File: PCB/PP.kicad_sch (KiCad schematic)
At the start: 22 parts, among them J1 USB_B_Micro, Q1 AO4425, Q2 AO3406, Q3 AO4425, Q4 AO3406, U1 ESP32-WROOM-32, U2 DRV8833PWP

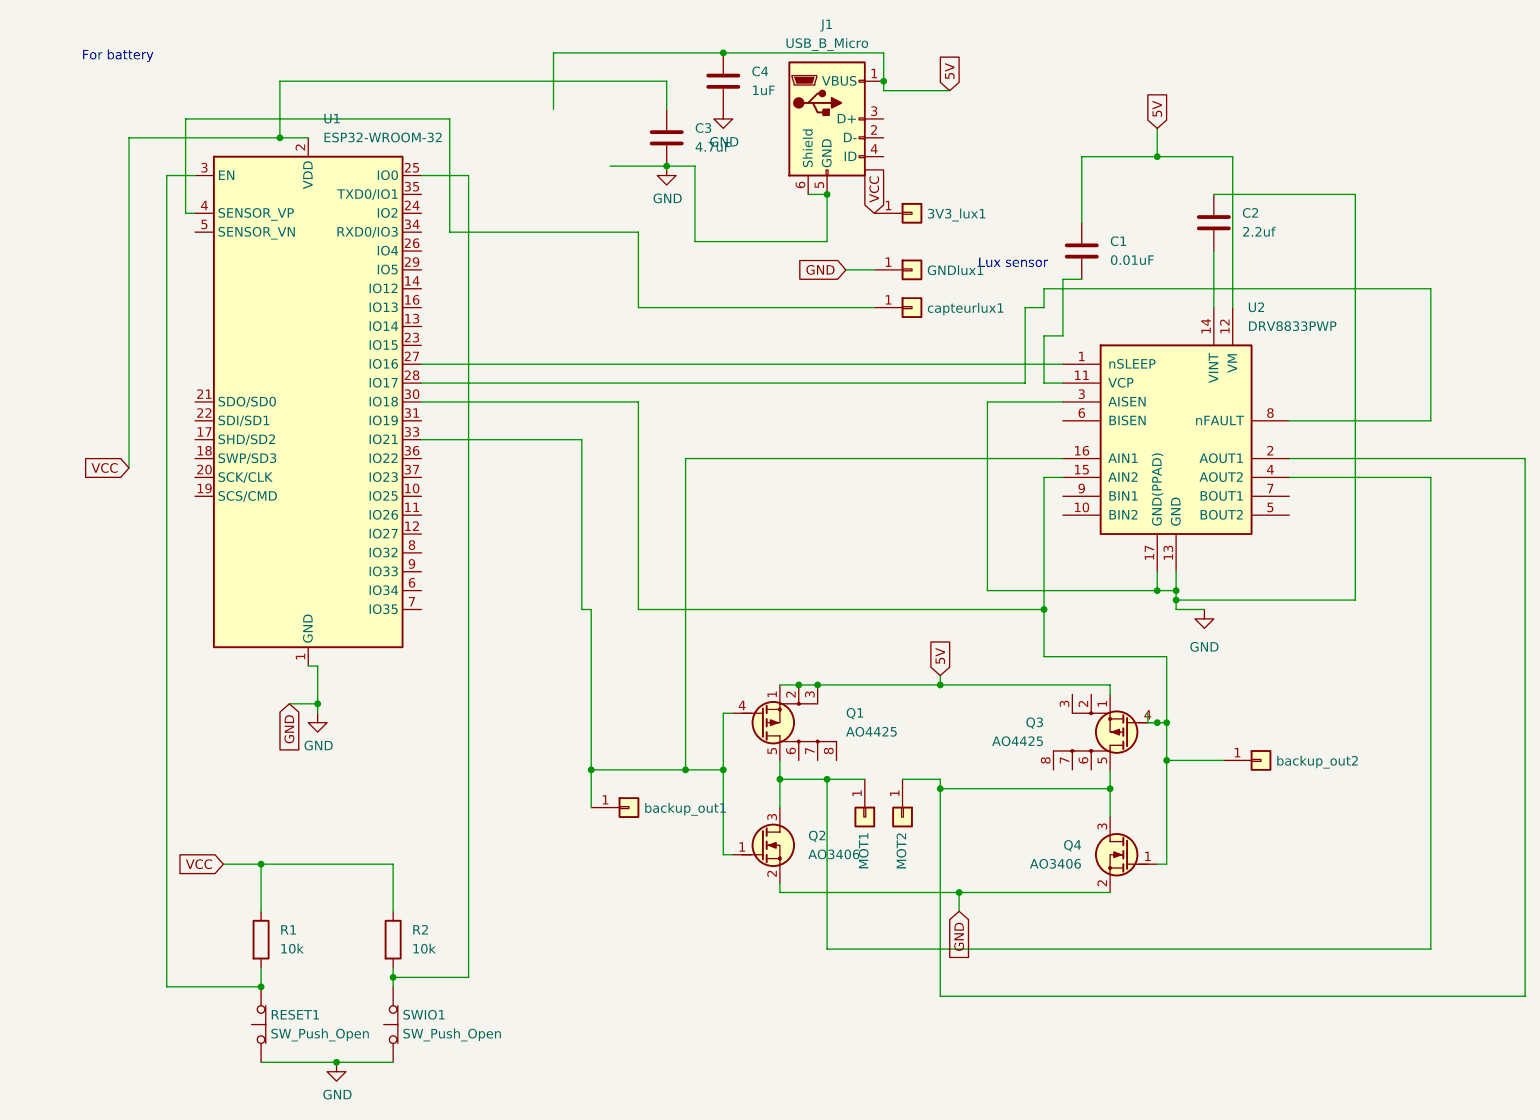
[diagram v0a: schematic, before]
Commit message: adding usb and ap7361 libs
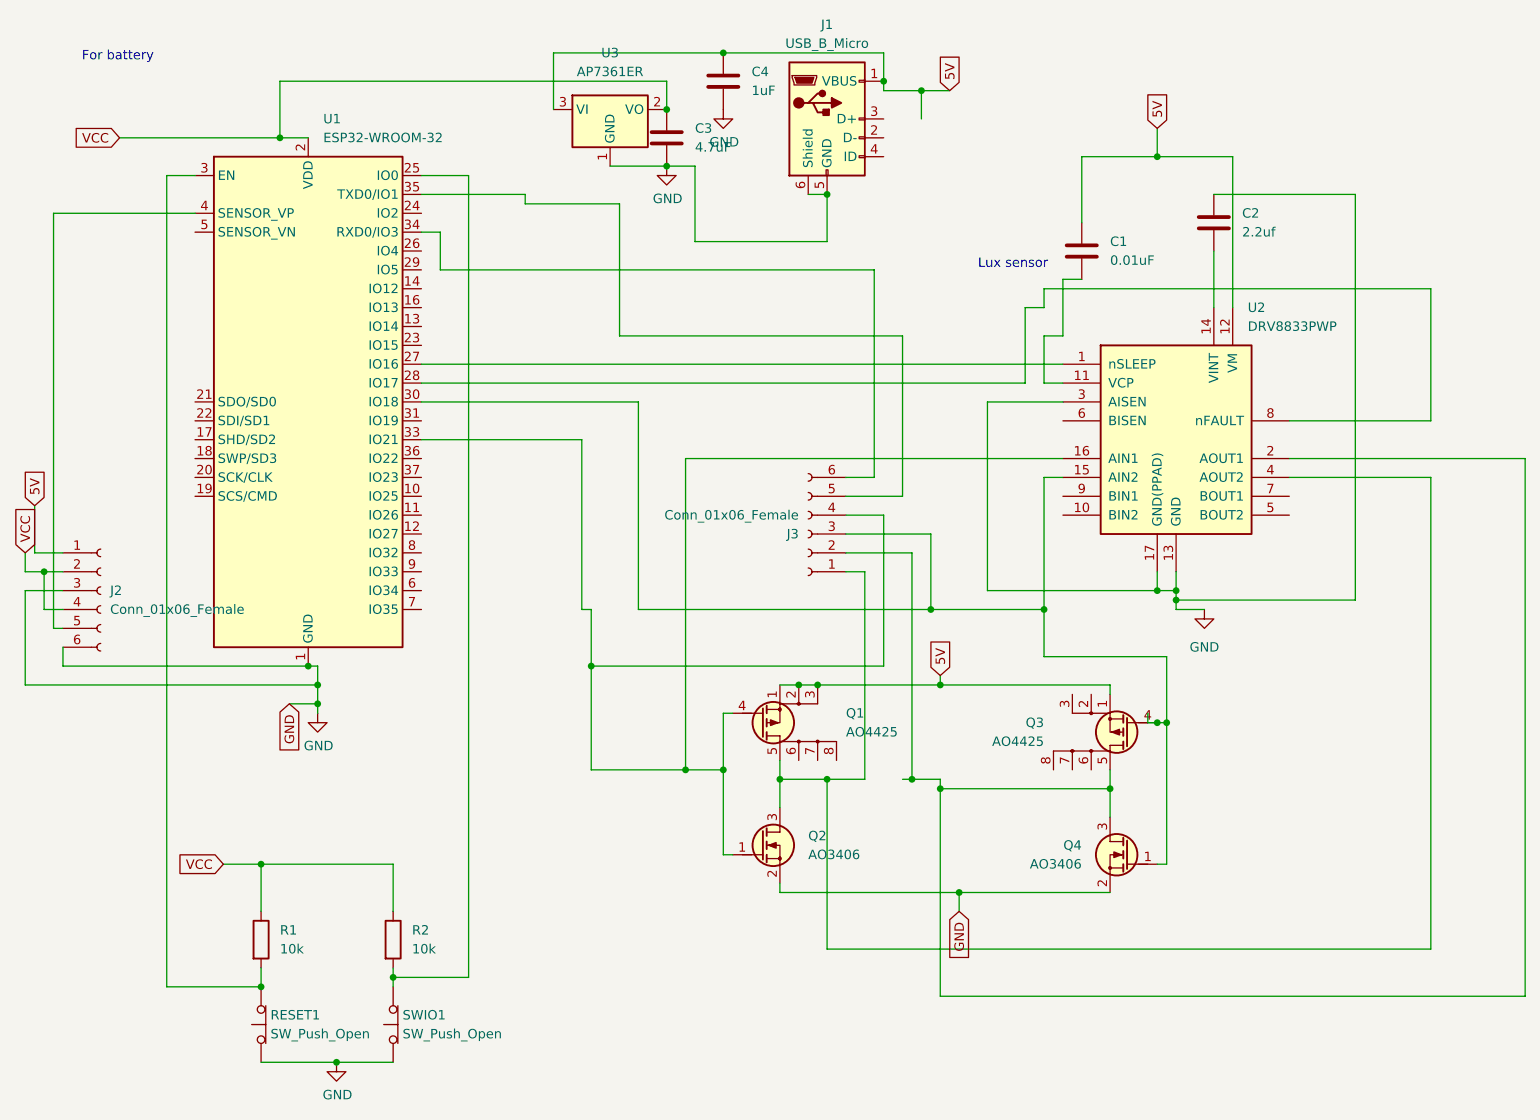
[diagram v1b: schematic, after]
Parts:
- removed 3V3_lux1, GNDlux1, MOT1, MOT2, backup_out1, backup_out2, capteurlux1: Conn_01x01, Connector_Pin:Pin_D1.2mm_L11.3mm_W3.0mm_Flat, symbol Connector_Generic:Conn_01x01
- added J2, J3: Conn_01x06_Female, TerminalBlock_Phoenix:TerminalBlock_Phoenix_MKDS-1,5-6_1x06_P5.00mm_Horizontal, symbol Connector:Conn_01x06_Female
- added U3: AP7361ER, Package_TO_SOT_SMD:SOT-223-3_TabPin2, symbol AP7361:AP7361ER
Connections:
- net 5V: now also J2.1 (Pin_1), U3.3 (VI)
- net GND: now also J2.3 (Pin_3), J2.6 (Pin_6), U3.1 (GND)
- net VCC: now also J2.2 (Pin_2), J2.4 (Pin_4), U3.2 (VO)
- net at U1.4 (SENSOR_VP): now also J2.5 (Pin_5)
- net at Q1.4 (G), Q2.1 (G), U1.33 (IO21)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: now also J3.4 (Pin_4)
- net at Q3.4 (G), Q4.1 (G), U1.30 (IO18)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: now also J3.3 (Pin_3)
- net at Q1.5 (D), Q2.3 (D), U2.4 (AOUT2): now also J3.1 (Pin_1)
- net at Q3.5 (D), Q4.3 (D), U2.2 (AOUT1): now also J3.2 (Pin_2)
- net at U1.34 (RXD0/IO3): now also J3.6 (Pin_6)
- net at U1.35 (TXD0/IO1): now also J3.5 (Pin_5)

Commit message: Update schematic & pcb v3
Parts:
- J1: footprint Connector_USB:USB_Micro-B_Wuerth_629105150521 -> usb:USB_aliexpress
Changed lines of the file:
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@@
     (property "Reference" "J1" (id 0) (at 121.92 10.16 0))
     (property "Value" "USB_B_Micro" (id 1) (at 121.92 12.7 0))
-    (property "Footprint" "Connector_USB:USB_Micro-B_Wuerth_629105150521" (id 2) (at 125.73 24.13 0)
+    (property "Footprint" "usb:USB_aliexpress" (id 2) (at 125.73 24.13 0)
       (effects (font (size 1.27 1.27)) hide)
     )
@@
     )
     (path "/91e4ba58-c38b-42d8-a298-d84c15b03b85"
-      (reference "J1") (unit 1) (value "USB_B_Micro") (footprint "Connector_USB:USB_Micro-B_Wuerth_629105150521")
+      (reference "J1") (unit 1) (value "USB_B_Micro") (footprint "usb:USB_aliexpress")
     )
     (path "/1d26900c-7759-4dc0-846e-9e4eb54777bf"
